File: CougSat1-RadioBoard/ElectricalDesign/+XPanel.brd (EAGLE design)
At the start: 79 x 90 mm, 65 parts, among them J1 ADCS Connector, J2 Low Gain +, J3 Low Gain -, J4 Low Gain Coax, J5 GPS Coax, J6 EPS Connector, U1 AD8515, U3 AD7291

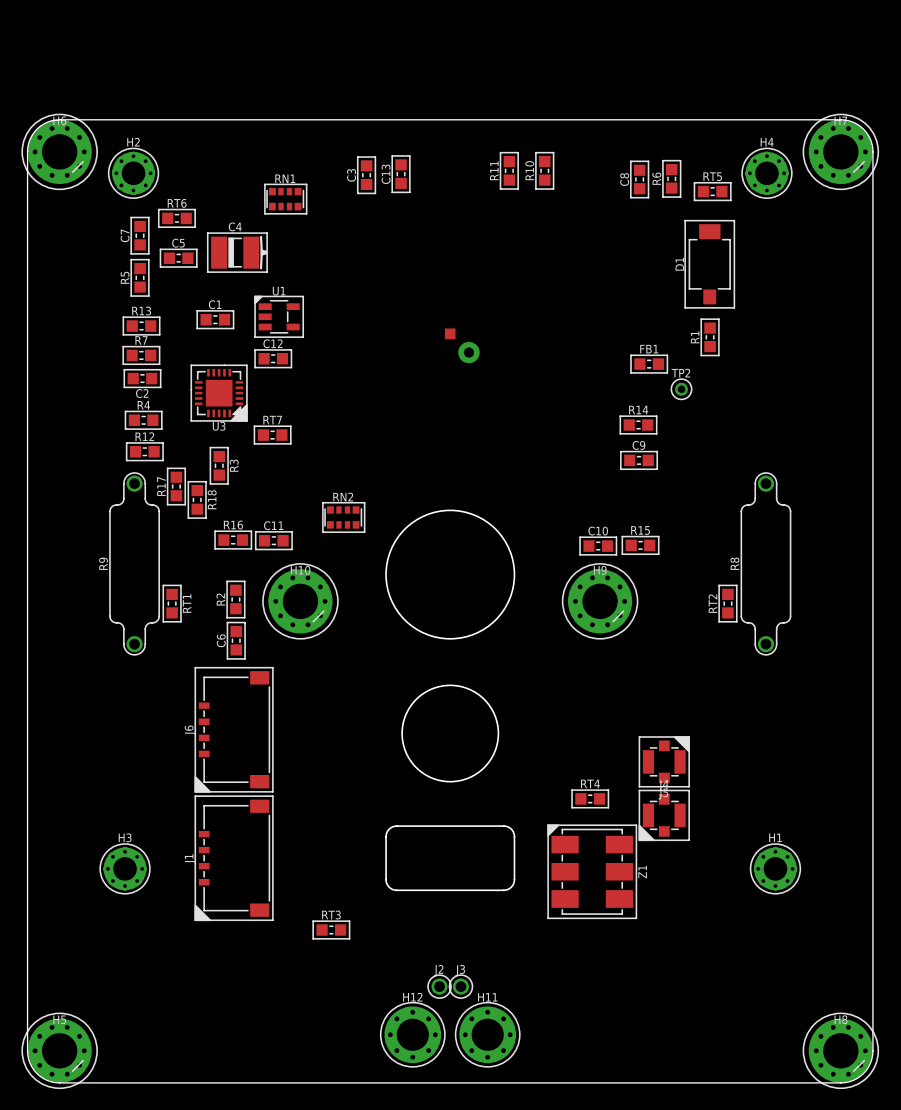
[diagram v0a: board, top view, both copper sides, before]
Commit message: Drew tKeepout for deployables
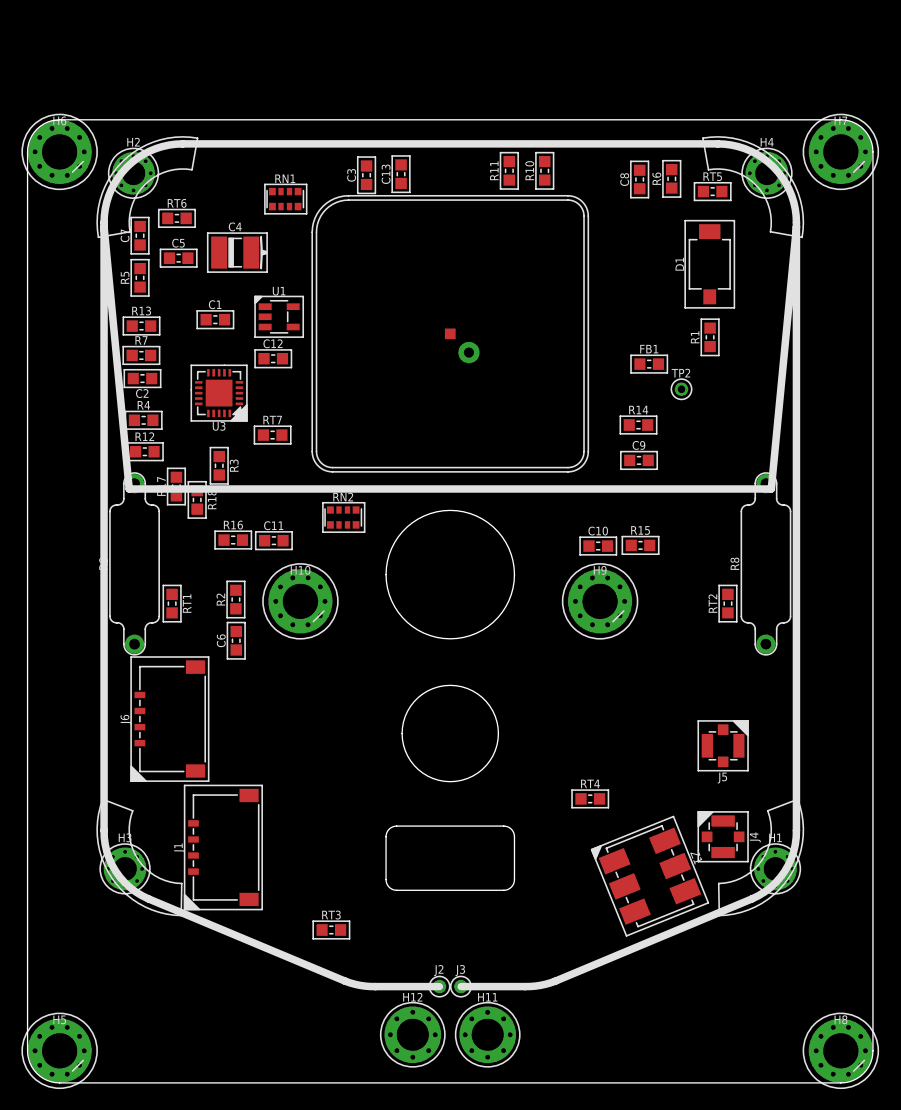
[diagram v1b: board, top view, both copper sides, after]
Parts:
- J2, J3: device CougsInSpace-Connectors:THT-1.0 -> CougsInSpace-Connectors:THT-0.7
- moved J6 6.08 mm to (-29.0, -11.0)
- moved J4 5.85 mm to (25.5, -22.0), turned to 270 degrees
- moved J5 5.70 mm to (25.5, -13.5)
- moved Z1 5.41 mm to (18.7, -25.7), turned to 292 degrees
- moved J1 1.41 mm to (-24.0, -23.0)
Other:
- outline, holes or cut-outs redrawn

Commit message: Moved Parts Out of Restricted Area
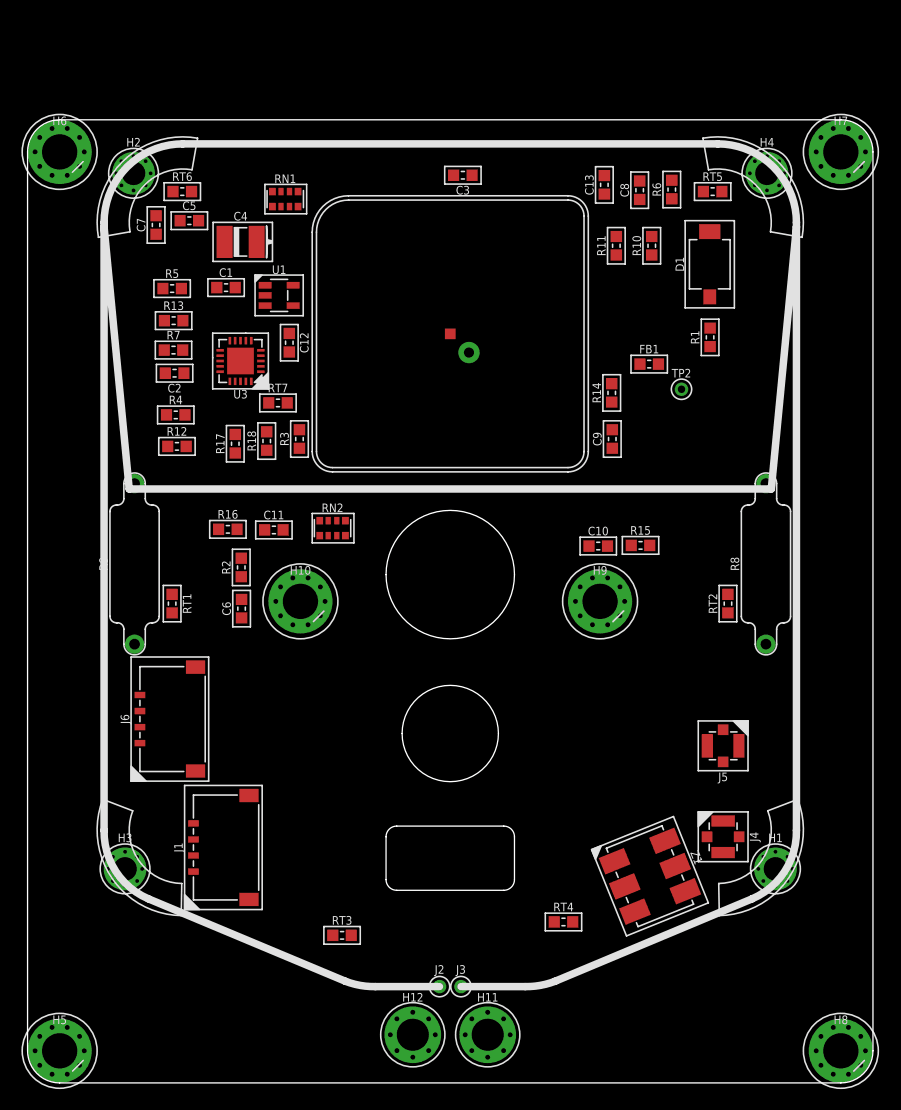
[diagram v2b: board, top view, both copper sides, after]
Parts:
- moved C13 19.0 mm to (14.4, 38.9)
- moved R11 12.2 mm to (15.5, 33.2)
- moved R10 12.2 mm to (18.8, 33.2)
- moved RT4 11.8 mm to (10.6, -30.0)
- moved C3 9.00 mm to (1.18, 39.8), turned to 180 degrees
- moved R18 8.51 mm to (-17.1, 15.0), turned to 90 degrees
- moved R3 7.91 mm to (-14.1, 15.2), turned to 90 degrees
- moved R17 6.80 mm to (-20.1, 14.7)
- moved R14 3.91 mm to (15.1, 19.5), turned to 90 degrees
- moved C5 3.64 mm to (-24.4, 35.6)
- moved U3 3.61 mm to (-19.6, 22.5)
- moved C9 3.20 mm to (15.1, 15.2), turned to 90 degrees
- moved C1 3.16 mm to (-20.9, 29.3)
- moved R5 3.16 mm to (-26.0, 29.2), turned to 0 degrees
- moved C2 3.04 mm to (-25.8, 21.3)
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
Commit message: Moved Patch Antenna
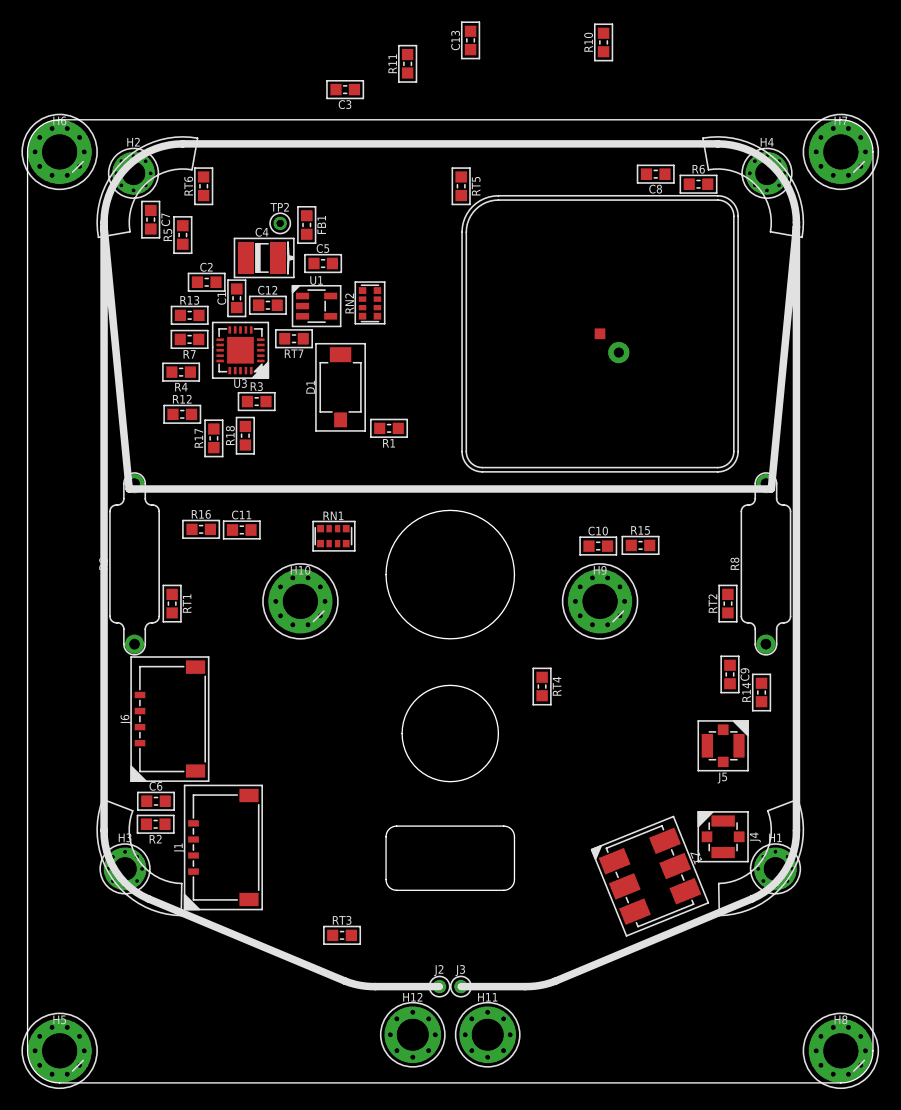
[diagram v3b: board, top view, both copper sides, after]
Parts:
- moved TP2 40.6 mm to (-15.9, 35.3)
- moved D1 36.4 mm to (-10.2, 20.0)
- moved FB1 34.5 mm to (-13.4, 35.2), turned to 270 degrees
- moved RN1 31.8 mm to (-10.9, 6.09)
- moved R14 31.3 mm to (29.1, -8.52)
- moved R1 31.2 mm to (-5.72, 16.2), turned to 180 degrees
- moved R11 25.9 mm to (-3.98, 50.2)
- moved R2 25.3 mm to (-27.5, -20.8), turned to 180 degrees
- moved C9 24.6 mm to (26.1, -6.83), turned to 270 degrees
- moved RT5 23.5 mm to (1.02, 38.8), turned to 270 degrees
- moved RT4 22.1 mm to (8.58, -7.96), turned to 270 degrees
- moved RN2 21.3 mm to (-7.50, 27.8), turned to 90 degrees
- moved C6 19.7 mm to (-27.5, -18.7), turned to 0 degrees
- moved R10 19.5 mm to (14.3, 52.2)
- moved C13 18.4 mm to (1.90, 52.4)
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
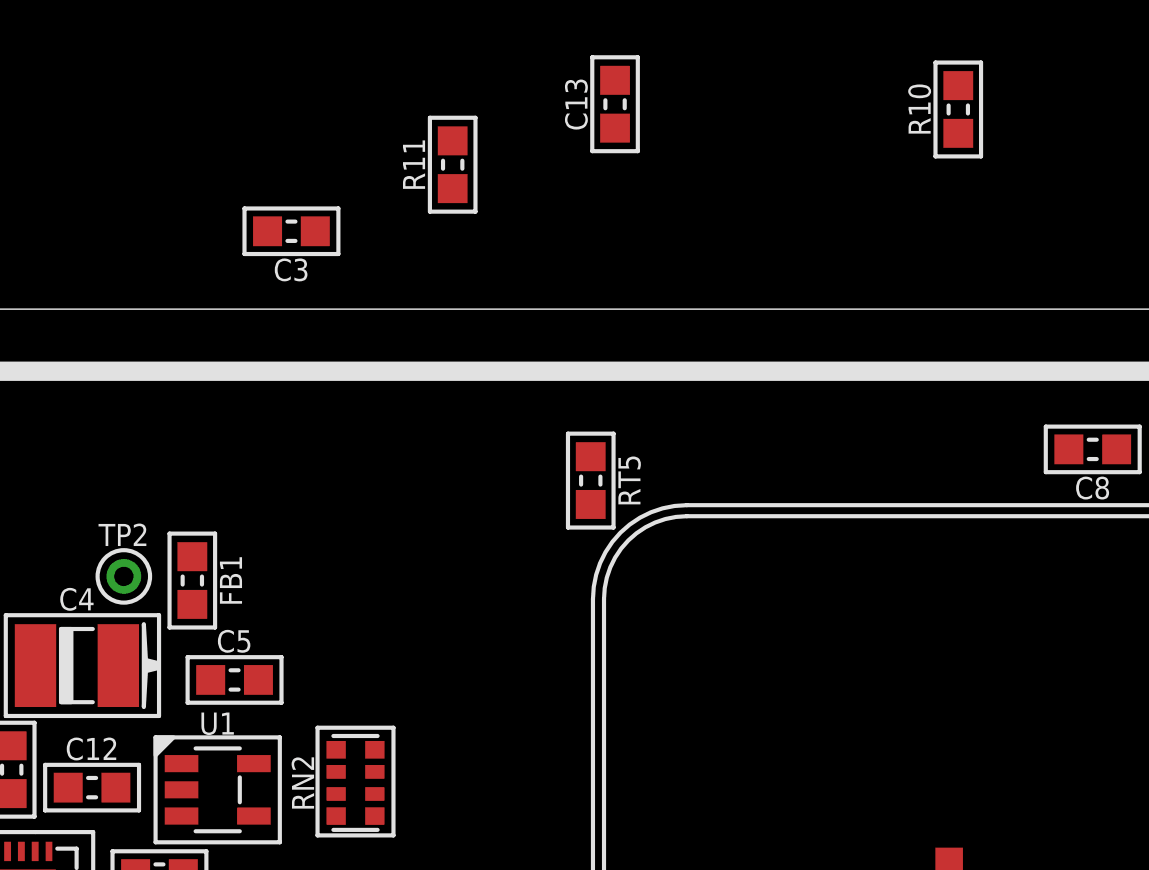
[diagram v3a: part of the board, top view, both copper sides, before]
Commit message: Moved decoupling capacitors
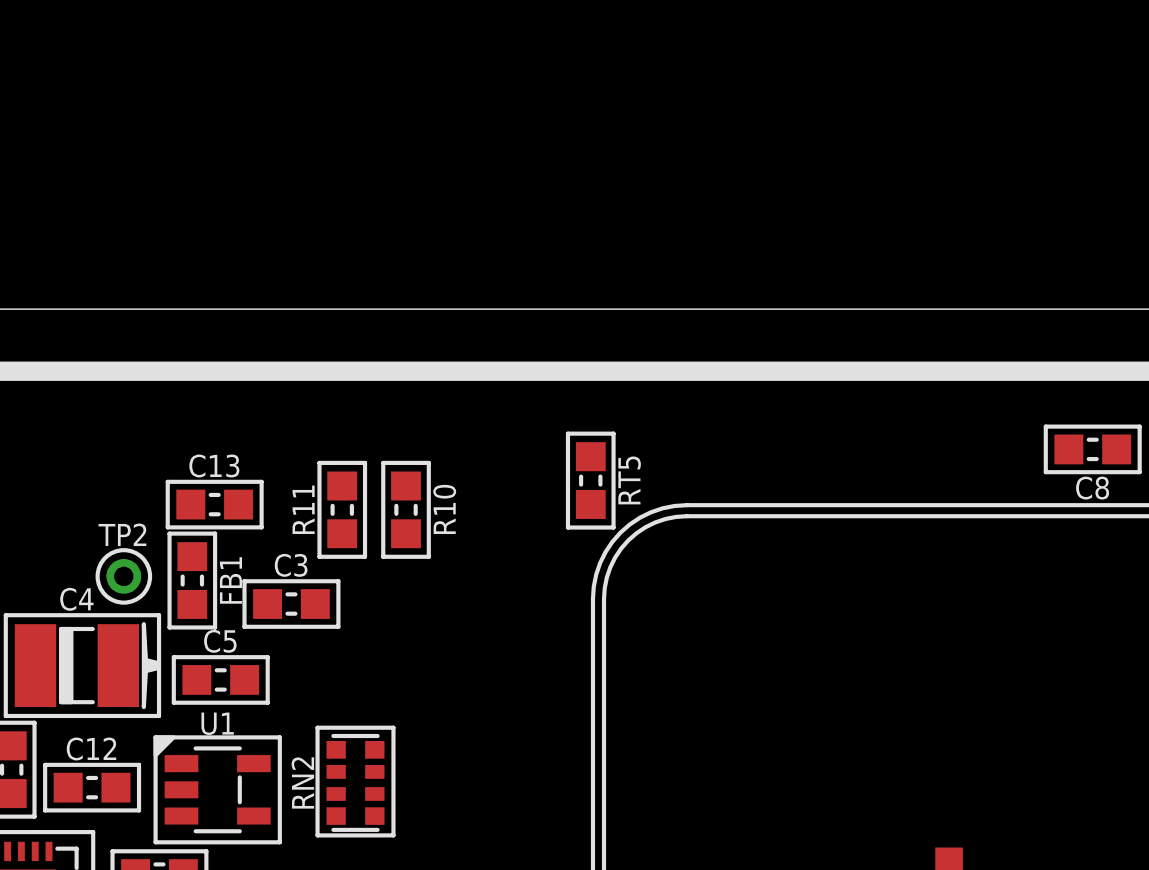
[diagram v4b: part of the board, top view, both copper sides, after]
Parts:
- moved R10 24.7 mm to (-5.67, 37.7), turned to 270 degrees
- moved C13 20.5 mm to (-12.6, 37.9), turned to 0 degrees
- moved C3 13.5 mm to (-9.82, 34.3), turned to 0 degrees
- moved R11 13.1 mm to (-7.98, 37.7)
- moved C5 0.50 mm to (-12.4, 31.6)

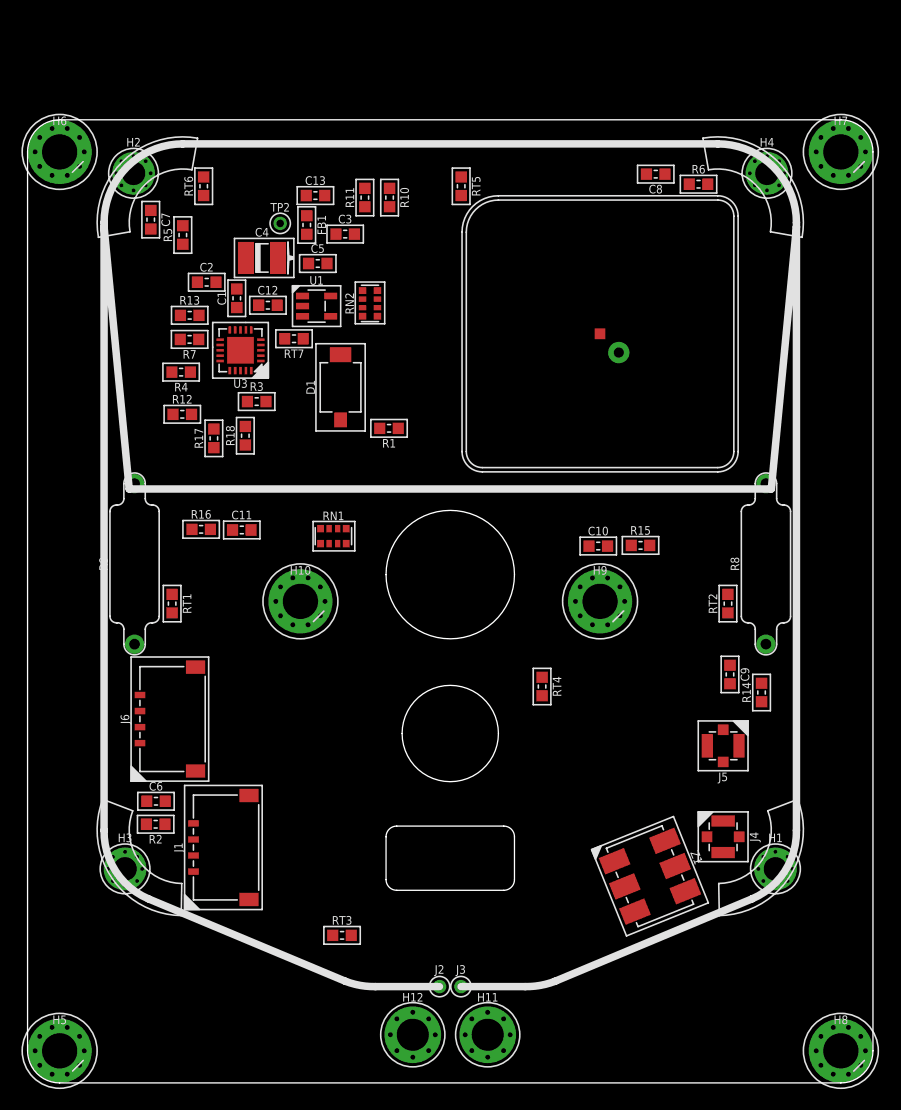
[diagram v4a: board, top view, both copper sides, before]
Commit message: Moved Capacitors
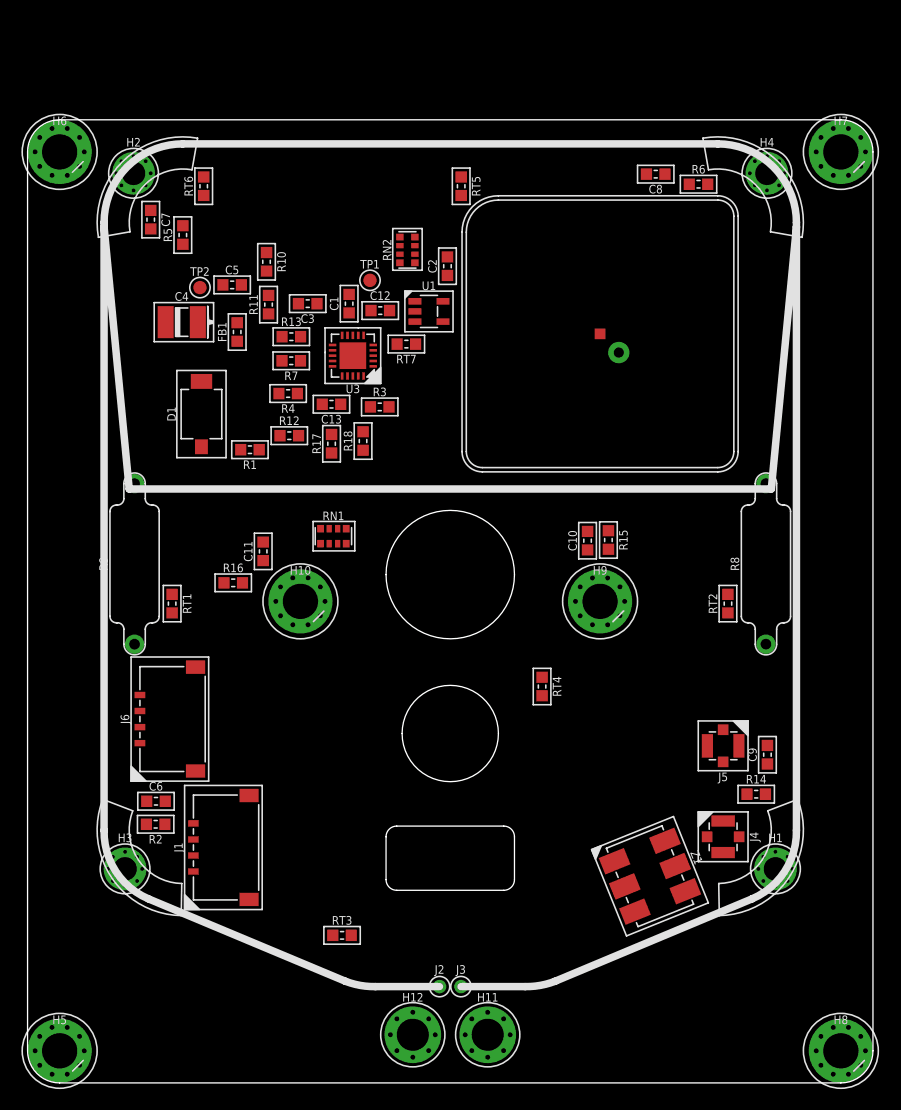
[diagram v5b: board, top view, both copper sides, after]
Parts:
- added TP1: TEST_POINT-SMD-C-1.25, CougsInSpace-Connectors:SMD-C-1.25
- TP2: value TEST_POINT-THT-0.7 -> TEST_POINT-SMD-C-1.25; device CougsInSpace-Connectors:THT-0.7 -> CougsInSpace-Connectors:SMD-C-1.25
- moved C2 22.5 mm to (-0.26, 31.3), turned to 90 degrees
- moved C13 19.6 mm to (-11.1, 18.4), turned to 180 degrees
- moved R11 13.5 mm to (-17.0, 27.7)
- moved D1 13.2 mm to (-23.2, 17.5)
- moved R1 13.2 mm to (-18.7, 14.2)
- moved R10 13.0 mm to (-17.2, 31.7)
- moved FB1 11.9 mm to (-19.9, 25.2), turned to 90 degrees
- moved R3 11.5 mm to (-6.59, 18.2)
- moved R17 11.0 mm to (-11.1, 14.7)
- moved R18 11.0 mm to (-8.15, 15.0)
- moved U3 10.5 mm to (-9.10, 23.0)
- moved C1 10.5 mm to (-9.45, 27.8)
- moved C12 10.5 mm to (-6.54, 27.2)
- moved RT7 10.5 mm to (-4.10, 24.0)
- moved U1 10.5 mm to (-1.99, 27.1)
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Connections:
- net AVREF_UNBUF: now also TP1.1
